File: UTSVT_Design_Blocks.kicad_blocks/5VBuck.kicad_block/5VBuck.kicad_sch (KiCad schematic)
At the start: 12 parts, among them U1 LMR51635XDDCR

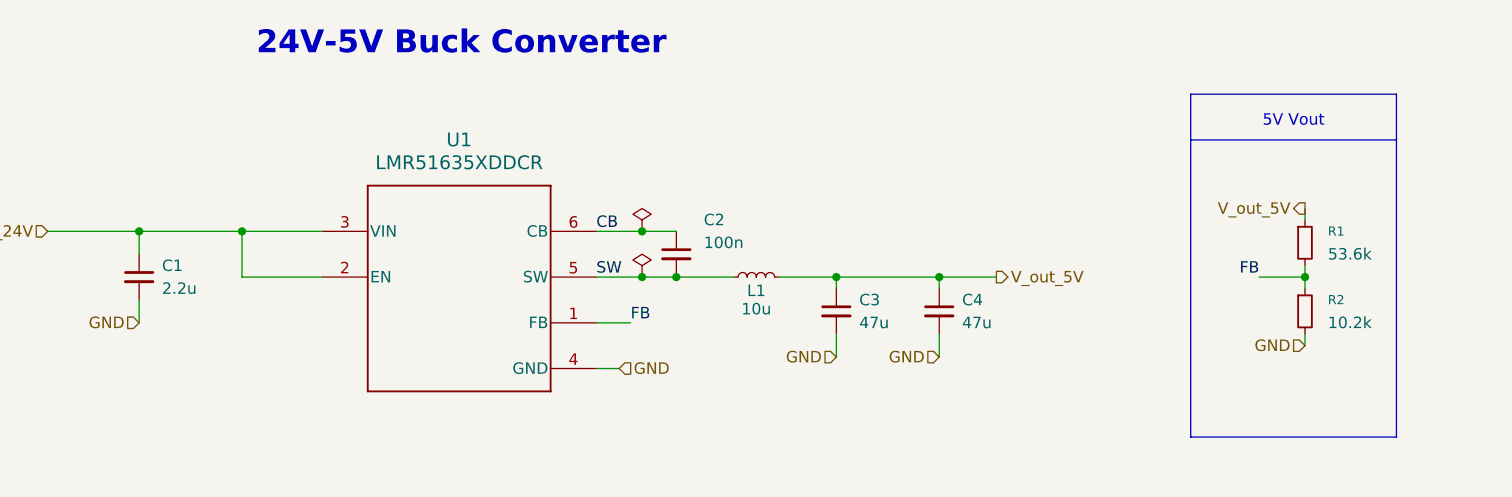
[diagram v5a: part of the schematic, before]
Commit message: updated resistor footprint from 0201 to 0603
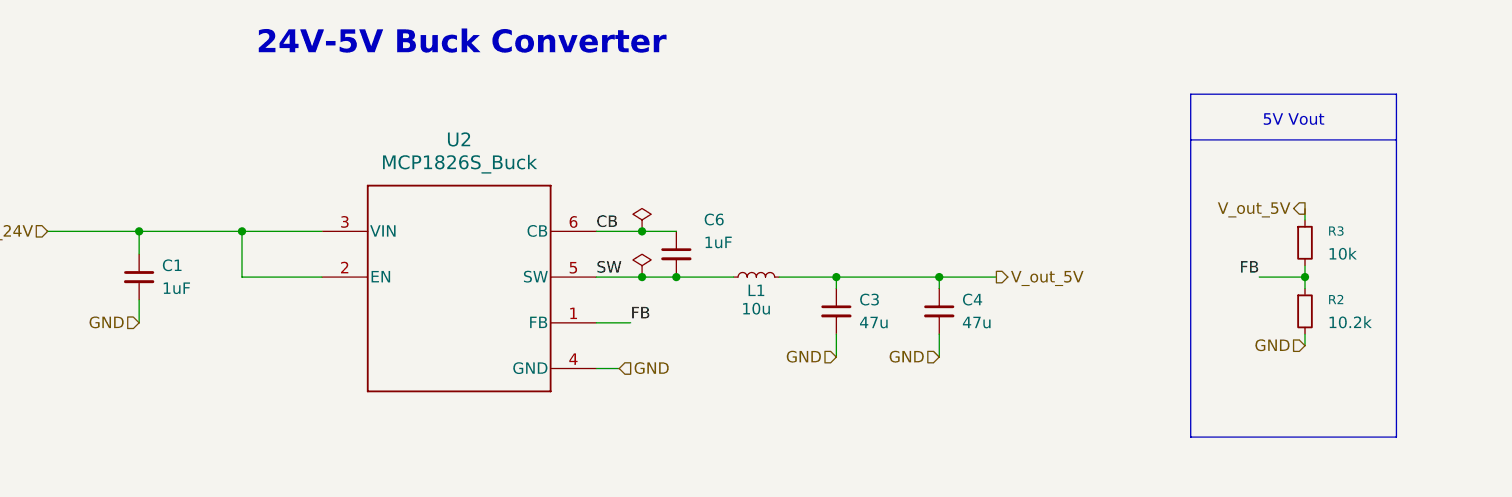
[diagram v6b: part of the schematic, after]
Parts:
- C1: value 2.2u -> 1uF
- C6: renamed from C2; value 100n -> 1uF
- R2: footprint Resistor_SMD:R_0201_0603Metric_Pad0.64x0.40mm_HandSolder -> Resistor_SMD:R_0603_1608Metric
- R3: renamed from R1; value 53.6k -> 10k; footprint Resistor_SMD:R_0201_0603Metric_Pad0.64x0.40mm_HandSolder -> Resistor_SMD:R_0603_1608Metric
- TP5, TP6, TP7, TP8: footprint (none) -> TestPoint:TestPoint_THTPad_D3.0mm_Drill1.5mm
- U2: renamed from U1; value LMR51635XDDCR -> MCP1826S_Buck; P/N LMR51635XDDCR -> MCP1826S
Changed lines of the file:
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@@
 			)
 		)
-		(property "Footprint" "Resistor_SMD:R_0201_0603Metric_Pad0.64x0.40mm_HandSolder"
+		(property "Footprint" "Resistor_SMD:R_0603_1608Metric"
 			(at 167.64 50.8 0)
 			(effects
@@
 			)
 		)
-		(property "Value" "2.2u"
+		(property "Value" "1uF"
 			(at 40.64 48.2662 0)
 			(effects
@@
 			)
 		)
-		(property "Footprint" ""
+		(property "Footprint" "TestPoint:TestPoint_THTPad_D3.0mm_Drill1.5mm"
 			(at 186.69 85.09 0)
 			(effects
@@
 		(on_board yes)
 		(dnp no)
-		(property "Reference" "C2"
+		(property "Reference" "C6"
 			(at 100.838 40.64 0)
 			(effects
@@
 			)
 		)
-		(property "Value" "100n"
+		(property "Value" "1uF"
 			(at 100.838 43.18 0)
 			(effects
@@
 			(project "5VBuck"
 				(path "/ad6c7df0-eb90-4670-9aa8-3e2007aefc2d/c59a1097-f91e-4d56-b57d-869363ca5893"
-					(reference "C2")
+					(reference "C6")
 					(unit 1)
 				)
@@
 		(dnp no)
 		(fields_autoplaced yes)
-		(property "Reference" "U1"
+		(property "Reference" "U2"
 			(at 73.66 31.75 0)
 			(effects
@@
 			)
 		)
-		(property "Value" "LMR51635XDDCR"
+		(property "Value" "MCP1826S_Buck"
 			(at 73.66 34.29 0)
 			(effects
@@
 			)
 		)
-		(property "Datasheet" "kicad-embed://lmr51635.pdf"
+		(property "Datasheet" "kicad-embed://MCP1826S.pdf"
 			(at 58.42 41.91 0)
 			(effects
@@
 			)
 		)
-		(property "P/N" "LMR51635XDDCR"
+		(property "P/N" "MCP1826S"
 			(at 58.42 41.91 0)
 			(effects
@@
 			(project "5VBuck"
 				(path "/ad6c7df0-eb90-4670-9aa8-3e2007aefc2d/c59a1097-f91e-4d56-b57d-869363ca5893"
-					(reference "U1")
+					(reference "U2")
 					(unit 1)
 				)
@@
 			)
 		)
-		(property "Footprint" ""
+		(property "Footprint" "TestPoint:TestPoint_THTPad_D3.0mm_Drill1.5mm"
 			(at 173.99 85.09 0)
 			(effects
@@
 			)
 		)
-		(property "Footprint" ""
+		(property "Footprint" "TestPoint:TestPoint_THTPad_D3.0mm_Drill1.5mm"
 			(at 186.69 97.79 0)
 			(effects
@@
 		(dnp no)
 		(fields_autoplaced yes)
-		(property "Reference" "R1"
+		(property "Reference" "R3"
 			(at 170.18 41.9099 0)
 			(effects
@@
 			)
 		)
-		(property "Value" "53.6k"
+		(property "Value" "10k"
 			(at 170.18 44.4499 0)
 			(effects
@@
 			)
 		)
-		(property "Footprint" "Resistor_SMD:R_0201_0603Metric_Pad0.64x0.40mm_HandSolder"
+		(property "Footprint" "Resistor_SMD:R_0603_1608Metric"
 			(at 167.64 43.18 0)
 			(effects
@@
 			(project "5VBuck"
 				(path "/ad6c7df0-eb90-4670-9aa8-3e2007aefc2d/c59a1097-f91e-4d56-b57d-869363ca5893"
-					(reference "R1")
+					(reference "R3")
 					(unit 1)
 				)
@@
 			)
 		)
-		(property "Footprint" ""
+		(property "Footprint" "TestPoint:TestPoint_THTPad_D3.0mm_Drill1.5mm"
 			(at 173.99 97.79 0)
 			(effects

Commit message: updated wrong resistor value
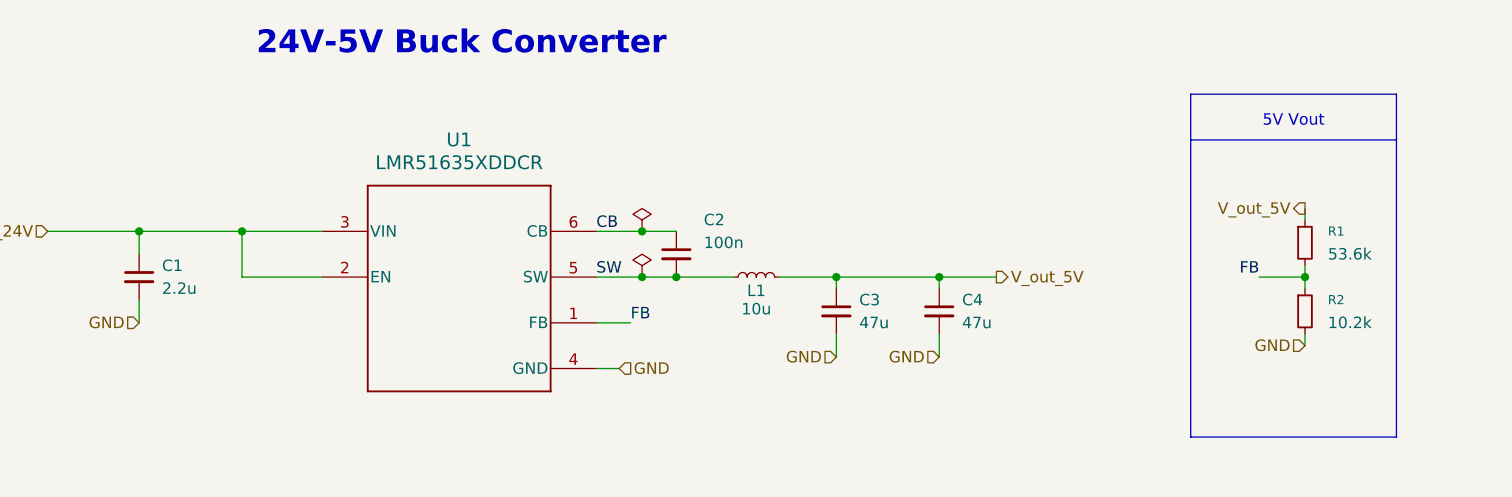
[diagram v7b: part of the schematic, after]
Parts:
- C1: value 1uF -> 2.2u
- C2: renamed from C6; value 1uF -> 100n
- R1: renamed from R3; value 10k -> 53.6k
- TP5, TP6, TP7, TP8: footprint TestPoint:TestPoint_THTPad_D3.0mm_Drill1.5mm -> (none)
- U1: renamed from U2; value MCP1826S_Buck -> LMR51635XDDCR; P/N MCP1826S -> LMR51635XDDCR
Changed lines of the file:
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@@
 			)
 			(project "5VBuck"
+				(path "/ad6c7df0-eb90-4670-9aa8-3e2007aefc2d/4ce3c563-64ba-4b6e-b334-e3956b5d5a33"
+					(reference "L1")
+					(unit 1)
+				)
 				(path "/ad6c7df0-eb90-4670-9aa8-3e2007aefc2d/c59a1097-f91e-4d56-b57d-869363ca5893"
 					(reference "L1")
@@
 			)
 			(project "5VBuck"
+				(path "/ad6c7df0-eb90-4670-9aa8-3e2007aefc2d/4ce3c563-64ba-4b6e-b334-e3956b5d5a33"
+					(reference "R2")
+					(unit 1)
+				)
 				(path "/ad6c7df0-eb90-4670-9aa8-3e2007aefc2d/c59a1097-f91e-4d56-b57d-869363ca5893"
 					(reference "R2")
@@
 			)
 		)
-		(property "Value" "1uF"
+		(property "Value" "2.2u"
 			(at 40.64 48.2662 0)
 			(effects
@@
 			)
 			(project "5VBuck"
+				(path "/ad6c7df0-eb90-4670-9aa8-3e2007aefc2d/4ce3c563-64ba-4b6e-b334-e3956b5d5a33"
+					(reference "C1")
+					(unit 1)
+				)
 				(path "/ad6c7df0-eb90-4670-9aa8-3e2007aefc2d/c59a1097-f91e-4d56-b57d-869363ca5893"
 					(reference "C1")
@@
 			)
 		)
-		(property "Footprint" "TestPoint:TestPoint_THTPad_D3.0mm_Drill1.5mm"
+		(property "Footprint" ""
 			(at 186.69 85.09 0)
 			(effects
@@
 		(instances
 			(project "PowerPath"
+				(path "/ad6c7df0-eb90-4670-9aa8-3e2007aefc2d/4ce3c563-64ba-4b6e-b334-e3956b5d5a33"
+					(reference "TP6")
+					(unit 1)
+				)
 				(path "/ad6c7df0-eb90-4670-9aa8-3e2007aefc2d/c59a1097-f91e-4d56-b57d-869363ca5893"
 					(reference "TP6")
@@
 		(on_board yes)
 		(dnp no)
-		(property "Reference" "C6"
+		(property "Reference" "C2"
 			(at 100.838 40.64 0)
 			(effects
@@
 			)
 		)
-		(property "Value" "1uF"
+		(property "Value" "100n"
 			(at 100.838 43.18 0)
 			(effects
@@
 			)
 			(project "5VBuck"
-				(path "/ad6c7df0-eb90-4670-9aa8-3e2007aefc2d/c59a1097-f91e-4d56-b57d-869363ca5893"
-					(reference "C6")
+				(path "/ad6c7df0-eb90-4670-9aa8-3e2007aefc2d/4ce3c563-64ba-4b6e-b334-e3956b5d5a33"
+					(reference "C2")
+					(unit 1)
+				)
+				(path "/ad6c7df0-eb90-4670-9aa8-3e2007aefc2d/c59a1097-f91e-4d56-b57d-869363ca5893"
+					(reference "C2")
 					(unit 1)
 				)
@@
 		(dnp no)
 		(fields_autoplaced yes)
-		(property "Reference" "U2"
+		(property "Reference" "U1"
 			(at 73.66 31.75 0)
 			(effects
@@
 			)
 		)
-		(property "Value" "MCP1826S_Buck"
+		(property "Value" "LMR51635XDDCR"
 			(at 73.66 34.29 0)
 			(effects
@@
 			)
 		)
-		(property "Datasheet" "kicad-embed://MCP1826S.pdf"
+		(property "Datasheet" "kicad-embed://lmr51635.pdf"
 			(at 58.42 41.91 0)
 			(effects
@@
 			)
 		)
-		(property "P/N" "MCP1826S"
+		(property "P/N" "LMR51635XDDCR"
 			(at 58.42 41.91 0)
 			(effects
@@
 			)
 			(project "5VBuck"
-				(path "/ad6c7df0-eb90-4670-9aa8-3e2007aefc2d/c59a1097-f91e-4d56-b57d-869363ca5893"
-					(reference "U2")
+				(path "/ad6c7df0-eb90-4670-9aa8-3e2007aefc2d/4ce3c563-64ba-4b6e-b334-e3956b5d5a33"
+					(reference "U1")
+					(unit 1)
+				)
+				(path "/ad6c7df0-eb90-4670-9aa8-3e2007aefc2d/c59a1097-f91e-4d56-b57d-869363ca5893"
+					(reference "U1")
 					(unit 1)
 				)
@@
 			)
 		)
-		(property "Footprint" "TestPoint:TestPoint_THTPad_D3.0mm_Drill1.5mm"
+		(property "Footprint" ""
 			(at 173.99 85.09 0)
 			(effects
@@
 		(instances
 			(project ""
+				(path "/ad6c7df0-eb90-4670-9aa8-3e2007aefc2d/4ce3c563-64ba-4b6e-b334-e3956b5d5a33"
+					(reference "TP5")
+					(unit 1)
+				)
 				(path "/ad6c7df0-eb90-4670-9aa8-3e2007aefc2d/c59a1097-f91e-4d56-b57d-869363ca5893"
 					(reference "TP5")
@@
 			)
 			(project "5VBuck"
+				(path "/ad6c7df0-eb90-4670-9aa8-3e2007aefc2d/4ce3c563-64ba-4b6e-b334-e3956b5d5a33"
+					(reference "#FLG01")
+					(unit 1)
+				)
 				(path "/ad6c7df0-eb90-4670-9aa8-3e2007aefc2d/c59a1097-f91e-4d56-b57d-869363ca5893"
 					(reference "#FLG01")
@@
 			)
 		)
-		(property "Footprint" "TestPoint:TestPoint_THTPad_D3.0mm_Drill1.5mm"
+		(property "Footprint" ""
 			(at 186.69 97.79 0)
 			(effects
@@
 		(instances
 			(project "PowerPath"
+				(path "/ad6c7df0-eb90-4670-9aa8-3e2007aefc2d/4ce3c563-64ba-4b6e-b334-e3956b5d5a33"
+					(reference "TP8")
+					(unit 1)
+				)
 				(path "/ad6c7df0-eb90-4670-9aa8-3e2007aefc2d/c59a1097-f91e-4d56-b57d-869363ca5893"
 					(reference "TP8")
@@
 			)
 			(project "5VBuck"
+				(path "/ad6c7df0-eb90-4670-9aa8-3e2007aefc2d/4ce3c563-64ba-4b6e-b334-e3956b5d5a33"
+					(reference "C4")
+					(unit 1)
+				)
 				(path "/ad6c7df0-eb90-4670-9aa8-3e2007aefc2d/c59a1097-f91e-4d56-b57d-869363ca5893"
 					(reference "C4")
@@
 			)
 			(project "5VBuck"
+				(path "/ad6c7df0-eb90-4670-9aa8-3e2007aefc2d/4ce3c563-64ba-4b6e-b334-e3956b5d5a33"
+					(reference "#FLG02")
+					(unit 1)
+				)
 				(path "/ad6c7df0-eb90-4670-9aa8-3e2007aefc2d/c59a1097-f91e-4d56-b57d-869363ca5893"
 					(reference "#FLG02")
@@
 		(dnp no)
 		(fields_autoplaced yes)
-		(property "Reference" "R3"
+		(property "Reference" "R1"
 			(at 170.18 41.9099 0)
 			(effects
@@
 			)
 		)
-		(property "Value" "10k"
+		(property "Value" "53.6k"
 			(at 170.18 44.4499 0)
 			(effects
@@
 			)
 			(project "5VBuck"
-				(path "/ad6c7df0-eb90-4670-9aa8-3e2007aefc2d/c59a1097-f91e-4d56-b57d-869363ca5893"
-					(reference "R3")
+				(path "/ad6c7df0-eb90-4670-9aa8-3e2007aefc2d/4ce3c563-64ba-4b6e-b334-e3956b5d5a33"
+					(reference "R1")
+					(unit 1)
+				)
+				(path "/ad6c7df0-eb90-4670-9aa8-3e2007aefc2d/c59a1097-f91e-4d56-b57d-869363ca5893"
+					(reference "R1")
 					(unit 1)
 				)
@@
 			)
 			(project "5VBuck"
+				(path "/ad6c7df0-eb90-4670-9aa8-3e2007aefc2d/4ce3c563-64ba-4b6e-b334-e3956b5d5a33"
+					(reference "C3")
+					(unit 1)
+				)
 				(path "/ad6c7df0-eb90-4670-9aa8-3e2007aefc2d/c59a1097-f91e-4d56-b57d-869363ca5893"
 					(reference "C3")
@@
 			)
 		)
-		(property "Footprint" "TestPoint:TestPoint_THTPad_D3.0mm_Drill1.5mm"
+		(property "Footprint" ""
 			(at 173.99 97.79 0)
 			(effects
@@
 		(instances
 			(project "PowerPath"
-				(path "/ad6c7df0-eb90-4670-9aa8-3e2007aefc2d/c59a1097-f91e-4d56-b57d-869363ca5893"
+				(path "/ad6c7df0-eb90-4670-9aa8-3e2007aefc2d/4ce3c563-64ba-4b6e-b334-e3956b5d5a33"
 					(reference "TP7")
+					(unit 1)
+				)
+				(path "/ad6c7df0-eb90-4670-9aa8-3e2007aefc2d/c59a1097-f91e-4d56-b57d-869363ca5893"
+					(reference "TP7")
